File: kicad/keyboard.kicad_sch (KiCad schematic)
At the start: 64 parts

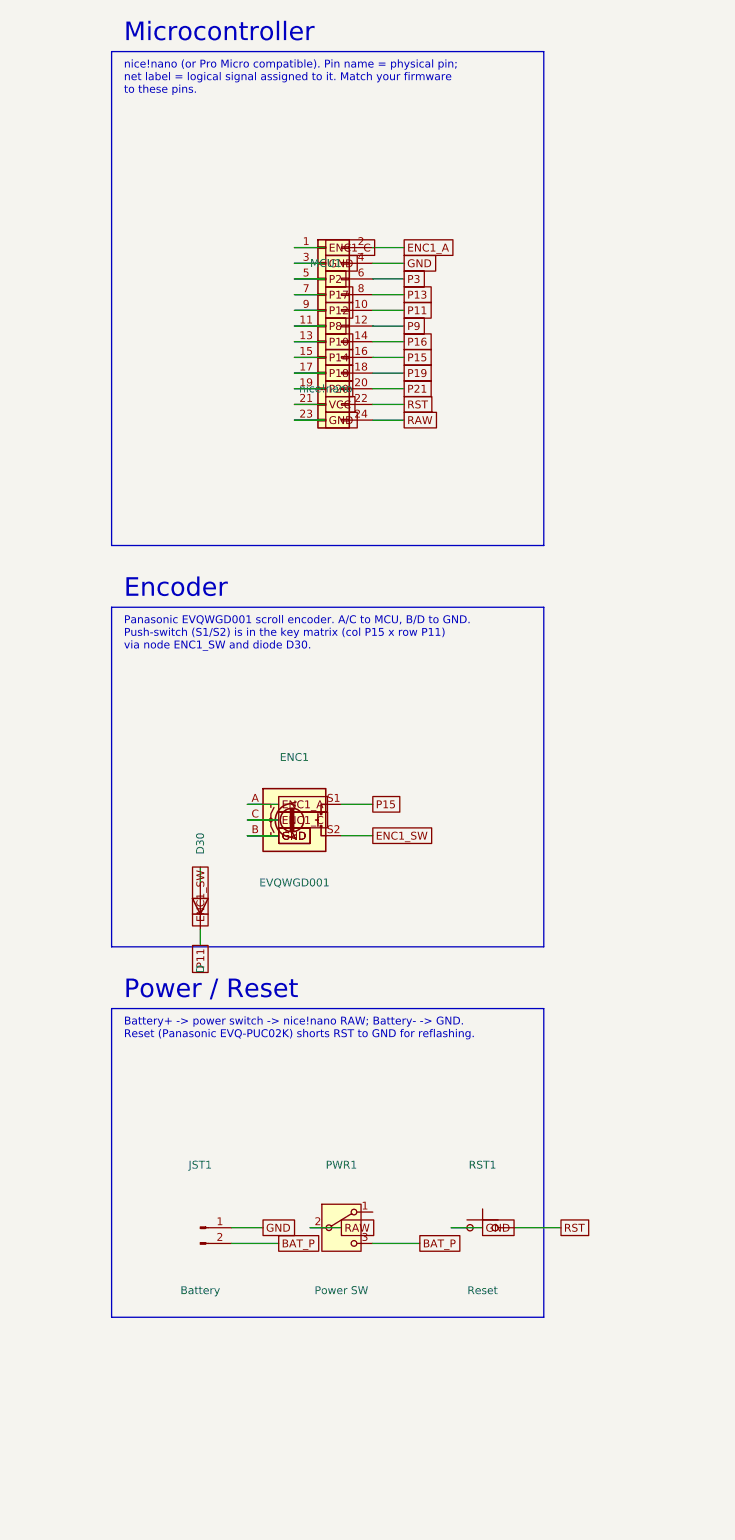
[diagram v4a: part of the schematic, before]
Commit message: Cleaner schematic layout: direction-aware pin wiring, more spacing
- Add pin_dir() + emit_pins_directional() so each symbol's pins leave along
  their real direction (encoder A/B/C left, S1/S2 right; SPDT power switch;
  nice!nano 2-column left/right) instead of all stubs going one way. This
  makes the encoder and power switch clearly wired (were ambiguous before).
- nice!nano uses non-staggered stubs so it reads as a clean 2-col DIP (was
  splaying into a leaf shape).
- Widen the MCU/Encoder/Power boxes and spread parts so nothing overlaps.
- Connectivity unchanged and verified (54 nets: matrix, encoder, power all
  correct).
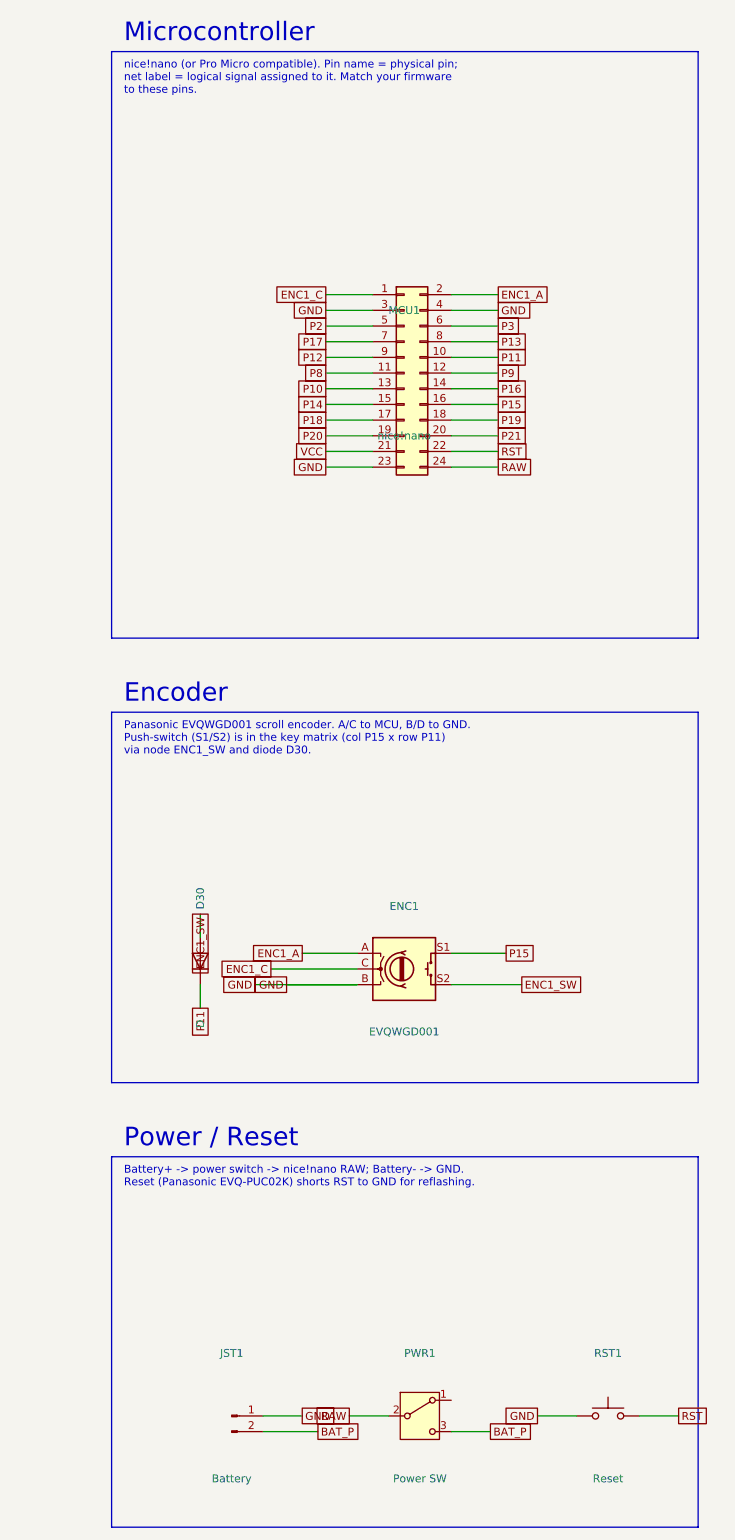
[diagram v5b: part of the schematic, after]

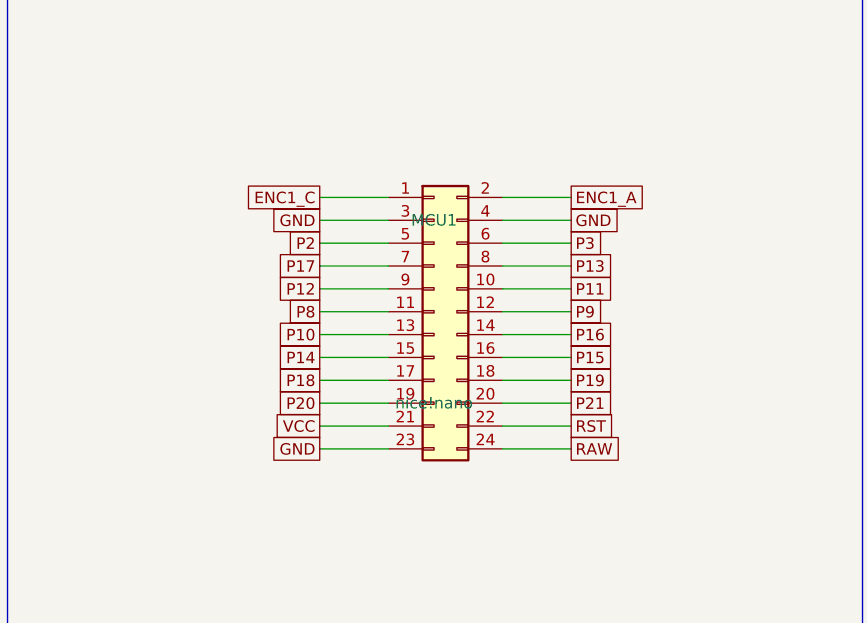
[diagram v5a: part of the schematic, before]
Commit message: Add physical pin names to the nice!nano symbol
Replace the generic 24-pin connector with a dedicated, generator-built
nice!nano symbol: a 2-column DIP body whose pins are labelled with their
real physical names (RAW, GND, VCC, P0-P21) matching the ceoloide
mcu_nice_nano footprint pad order. Pad numbering still matches
Conn_02x12_Odd_Even so the pad->net wiring is unchanged.

Now each pin reads clearly (physical pin name on the symbol, logical net
label on the stub) like the reference schematic's ProMicro. Connectivity
verified unchanged (54 nets).
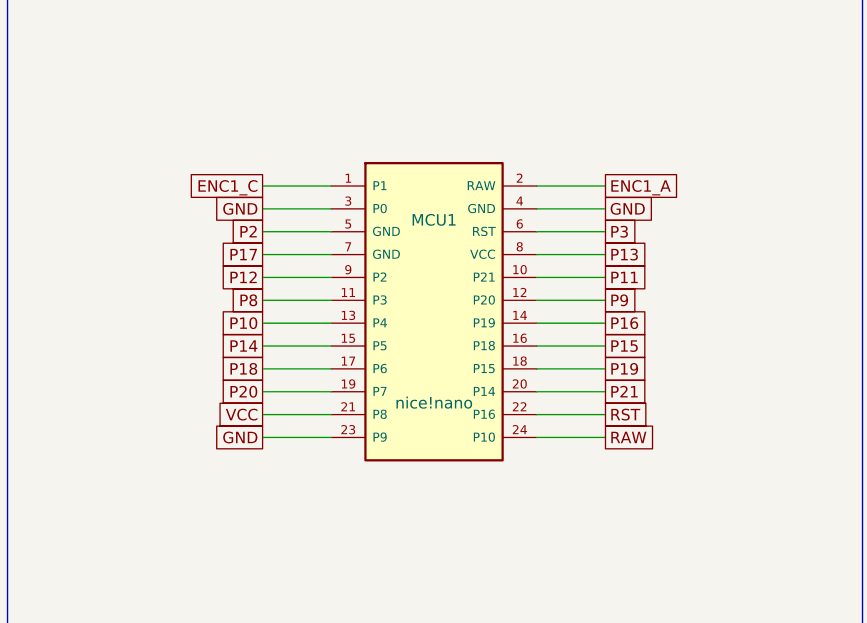
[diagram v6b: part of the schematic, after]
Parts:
- removed MCU1: nice!nano, symbol Connector_Generic:Conn_02x12_Odd_Even
- added MCU1: nice!nano, symbol keeb:nice_nano
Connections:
- net ENC1_A: now also MCU1.2 (RAW)
- net ENC1_C: now also MCU1.1 (P1)
- net GND: now also MCU1.23 (P9), MCU1.3 (P0), MCU1.4 (GND)
- net P10: now also MCU1.13 (P4)
- net P11: now also MCU1.10 (P21)
- net P12: now also MCU1.9 (P2)
- net P13: now also MCU1.8 (VCC)
- net P14: now also MCU1.15 (P5)
- net P15: now also MCU1.16 (P18)
- net P16: now also MCU1.14 (P19)
- net P17: now also MCU1.7 (GND)
- net P18: now also MCU1.17 (P6)
- net P19: now also MCU1.18 (P15)
- net P2: now also MCU1.5 (GND)
- net P20: now also MCU1.19 (P7)
- net P21: now also MCU1.20 (P14)
- net P3: now also MCU1.6 (RST)
- net P8: now also MCU1.11 (P3)
- net P9: now also MCU1.12 (P20)
- net RAW: now also MCU1.24 (P10)
- net RST: now also MCU1.22 (P16)
- net VCC: now also MCU1.21 (P8)
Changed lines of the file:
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@@
   (text "nice!nano (or Pro Micro compatible). Pin name = physical pin;\nnet label = logical signal assigned to it. Match your firmware\nto these pins." (at 268.30 31.98 0)
     (effects (font (size 1.27 1.27)) (justify left top)))
-  (symbol (lib_id "Connector_Generic:Conn_02x12_Odd_Even") (at 313.69 82.55 0) (unit 1)
+  (symbol (lib_id "keeb:nice_nano") (at 313.69 82.55 0) (unit 1)
     (in_bom yes) (on_board yes) (dnp no)
     (property "Reference" "MCU1" (at 313.69 72.39 0)
@@
       (effects (font (size 1.27 1.27))))
   )
-  (wire (pts (xy 321.31 97.79) (xy 328.93 97.79)) (stroke (width 0) (type default)))
-  (global_label "RAW" (shape passive) (at 328.93 97.79 0)
+  (wire (pts (xy 325.12 96.52) (xy 332.74 96.52)) (stroke (width 0) (type default)))
+  (global_label "RAW" (shape passive) (at 332.74 96.52 0)
     (effects (font (size 1.27 1.27)) (justify left)))
-  (wire (pts (xy 308.61 69.85) (xy 300.99 69.85)) (stroke (width 0) (type default)))
-  (global_label "ENC1_C" (shape passive) (at 300.99 69.85 0)
+  (wire (pts (xy 302.26 68.58) (xy 294.64 68.58)) (stroke (width 0) (type default)))
+  (global_label "ENC1_C" (shape passive) (at 294.64 68.58 0)
     (effects (font (size 1.27 1.27)) (justify right)))
-  (wire (pts (xy 308.61 97.79) (xy 300.99 97.79)) (stroke (width 0) (type default)))
-  (global_label "GND" (shape passive) (at 300.99 97.79 0)
+  (wire (pts (xy 302.26 96.52) (xy 294.64 96.52)) (stroke (width 0) (type default)))
+  (global_label "GND" (shape passive) (at 294.64 96.52 0)
     (effects (font (size 1.27 1.27)) (justify right)))
-  (wire (pts (xy 321.31 69.85) (xy 328.93 69.85)) (stroke (width 0) (type default)))
-  (global_label "ENC1_A" (shape passive) (at 328.93 69.85 0)
+  (wire (pts (xy 325.12 68.58) (xy 332.74 68.58)) (stroke (width 0) (type default)))
+  (global_label "ENC1_A" (shape passive) (at 332.74 68.58 0)
     (effects (font (size 1.27 1.27)) (justify left)))
-  (wire (pts (xy 321.31 95.25) (xy 328.93 95.25)) (stroke (width 0) (type default)))
-  (global_label "RST" (shape passive) (at 328.93 95.25 0)
+  (wire (pts (xy 325.12 93.98) (xy 332.74 93.98)) (stroke (width 0) (type default)))
+  (global_label "RST" (shape passive) (at 332.74 93.98 0)
     (effects (font (size 1.27 1.27)) (justify left)))
-  (wire (pts (xy 308.61 72.39) (xy 300.99 72.39)) (stroke (width 0) (type default)))
-  (global_label "GND" (shape passive) (at 300.99 72.39 0)
+  (wire (pts (xy 302.26 71.12) (xy 294.64 71.12)) (stroke (width 0) (type default)))
+  (global_label "GND" (shape passive) (at 294.64 71.12 0)
     (effects (font (size 1.27 1.27)) (justify right)))
-  (wire (pts (xy 308.61 95.25) (xy 300.99 95.25)) (stroke (width 0) (type default)))
-  (global_label "VCC" (shape passive) (at 300.99 95.25 0)
+  (wire (pts (xy 302.26 93.98) (xy 294.64 93.98)) (stroke (width 0) (type default)))
+  (global_label "VCC" (shape passive) (at 294.64 93.98 0)
     (effects (font (size 1.27 1.27)) (justify right)))
-  (wire (pts (xy 321.31 72.39) (xy 328.93 72.39)) (stroke (width 0) (type default)))
-  (global_label "GND" (shape passive) (at 328.93 72.39 0)
+  (wire (pts (xy 325.12 71.12) (xy 332.74 71.12)) (stroke (width 0) (type default)))
+  (global_label "GND" (shape passive) (at 332.74 71.12 0)
     (effects (font (size 1.27 1.27)) (justify left)))
-  (wire (pts (xy 321.31 92.71) (xy 328.93 92.71)) (stroke (width 0) (type default)))
-  (global_label "P21" (shape passive) (at 328.93 92.71 0)
+  (wire (pts (xy 325.12 91.44) (xy 332.74 91.44)) (stroke (width 0) (type default)))
+  (global_label "P21" (shape passive) (at 332.74 91.44 0)
     (effects (font (size 1.27 1.27)) (justify left)))
-  (wire (pts (xy 308.61 74.93) (xy 300.99 74.93)) (stroke (width 0) (type default)))
-  (global_label "P2" (shape passive) (at 300.99 74.93 0)
+  (wire (pts (xy 302.26 73.66) (xy 294.64 73.66)) (stroke (width 0) (type default)))
+  (global_label "P2" (shape passive) (at 294.64 73.66 0)
     (effects (font (size 1.27 1.27)) (justify right)))
-  (wire (pts (xy 308.61 92.71) (xy 300.99 92.71)) (stroke (width 0) (type default)))
-  (global_label "P20" (shape passive) (at 300.99 92.71 0)
+  (wire (pts (xy 302.26 91.44) (xy 294.64 91.44)) (stroke (width 0) (type default)))
+  (global_label "P20" (shape passive) (at 294.64 91.44 0)
     (effects (font (size 1.27 1.27)) (justify right)))
-  (wire (pts (xy 321.31 74.93) (xy 328.93 74.93)) (stroke (width 0) (type default)))
-  (global_label "P3" (shape passive) (at 328.93 74.93 0)
+  (wire (pts (xy 325.12 73.66) (xy 332.74 73.66)) (stroke (width 0) (type default)))
+  (global_label "P3" (shape passive) (at 332.74 73.66 0)
     (effects (font (size 1.27 1.27)) (justify left)))
-  (wire (pts (xy 321.31 90.17) (xy 328.93 90.17)) (stroke (width 0) (type default)))
-  (global_label "P19" (shape passive) (at 328.93 90.17 0)
+  (wire (pts (xy 325.12 88.90) (xy 332.74 88.90)) (stroke (width 0) (type default)))
+  (global_label "P19" (shape passive) (at 332.74 88.90 0)
     (effects (font (size 1.27 1.27)) (justify left)))
-  (wire (pts (xy 308.61 77.47) (xy 300.99 77.47)) (stroke (width 0) (type default)))
-  (global_label "P17" (shape passive) (at 300.99 77.47 0)
+  (wire (pts (xy 302.26 76.20) (xy 294.64 76.20)) (stroke (width 0) (type default)))
+  (global_label "P17" (shape passive) (at 294.64 76.20 0)
     (effects (font (size 1.27 1.27)) (justify right)))
-  (wire (pts (xy 308.61 90.17) (xy 300.99 90.17)) (stroke (width 0) (type default)))
-  (global_label "P18" (shape passive) (at 300.99 90.17 0)
+  (wire (pts (xy 302.26 88.90) (xy 294.64 88.90)) (stroke (width 0) (type default)))
+  (global_label "P18" (shape passive) (at 294.64 88.90 0)
     (effects (font (size 1.27 1.27)) (justify right)))
-  (wire (pts (xy 321.31 77.47) (xy 328.93 77.47)) (stroke (width 0) (type default)))
-  (global_label "P13" (shape passive) (at 328.93 77.47 0)
+  (wire (pts (xy 325.12 76.20) (xy 332.74 76.20)) (stroke (width 0) (type default)))
+  (global_label "P13" (shape passive) (at 332.74 76.20 0)
     (effects (font (size 1.27 1.27)) (justify left)))
-  (wire (pts (xy 321.31 87.63) (xy 328.93 87.63)) (stroke (width 0) (type default)))
-  (global_label "P15" (shape passive) (at 328.93 87.63 0)
+  (wire (pts (xy 325.12 86.36) (xy 332.74 86.36)) (stroke (width 0) (type default)))
+  (global_label "P15" (shape passive) (at 332.74 86.36 0)
     (effects (font (size 1.27 1.27)) (justify left)))
-  (wire (pts (xy 308.61 80.01) (xy 300.99 80.01)) (stroke (width 0) (type default)))
-  (global_label "P12" (shape passive) (at 300.99 80.01 0)
+  (wire (pts (xy 302.26 78.74) (xy 294.64 78.74)) (stroke (width 0) (type default)))
+  (global_label "P12" (shape passive) (at 294.64 78.74 0)
     (effects (font (size 1.27 1.27)) (justify right)))
-  (wire (pts (xy 308.61 87.63) (xy 300.99 87.63)) (stroke (width 0) (type default)))
-  (global_label "P14" (shape passive) (at 300.99 87.63 0)
+  (wire (pts (xy 302.26 86.36) (xy 294.64 86.36)) (stroke (width 0) (type default)))
+  (global_label "P14" (shape passive) (at 294.64 86.36 0)
     (effects (font (size 1.27 1.27)) (justify right)))
-  (wire (pts (xy 321.31 80.01) (xy 328.93 80.01)) (stroke (width 0) (type default)))
-  (global_label "P11" (shape passive) (at 328.93 80.01 0)
+  (wire (pts (xy 325.12 78.74) (xy 332.74 78.74)) (stroke (width 0) (type default)))
+  (global_label "P11" (shape passive) (at 332.74 78.74 0)
     (effects (font (size 1.27 1.27)) (justify left)))
-  (wire (pts (xy 321.31 85.09) (xy 328.93 85.09)) (stroke (width 0) (type default)))
-  (global_label "P16" (shape passive) (at 328.93 85.09 0)
+  (wire (pts (xy 325.12 83.82) (xy 332.74 83.82)) (stroke (width 0) (type default)))
+  (global_label "P16" (shape passive) (at 332.74 83.82 0)
     (effects (font (size 1.27 1.27)) (justify left)))
-  (wire (pts (xy 308.61 82.55) (xy 300.99 82.55)) (stroke (width 0) (type default)))
-  (global_label "P8" (shape passive) (at 300.99 82.55 0)
+  (wire (pts (xy 302.26 81.28) (xy 294.64 81.28)) (stroke (width 0) (type default)))
+  (global_label "P8" (shape passive) (at 294.64 81.28 0)
     (effects (font (size 1.27 1.27)) (justify right)))
-  (wire (pts (xy 308.61 85.09) (xy 300.99 85.09)) (stroke (width 0) (type default)))
-  (global_label "P10" (shape passive) (at 300.99 85.09 0)
+  (wire (pts (xy 302.26 83.82) (xy 294.64 83.82)) (stroke (width 0) (type default)))
+  (global_label "P10" (shape passive) (at 294.64 83.82 0)
     (effects (font (size 1.27 1.27)) (justify right)))
-  (wire (pts (xy 321.31 82.55) (xy 328.93 82.55)) (stroke (width 0) (type default)))
-  (global_label "P9" (shape passive) (at 328.93 82.55 0)
+  (wire (pts (xy 325.12 81.28) (xy 332.74 81.28)) (stroke (width 0) (type default)))
+  (global_label "P9" (shape passive) (at 332.74 81.28 0)
     (effects (font (size 1.27 1.27)) (justify left)))
   (rectangle (start 266.30 137.48) (end 361.30 197.48)
